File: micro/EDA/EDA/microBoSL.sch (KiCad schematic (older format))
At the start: 51 parts, among them J1 Conn_01x04, J10 MOTOR_OUT, J2 Conn_01x03, J3 Conn_01x04, J4 BATTERY CONN, J5 Conn_02x03_Odd_Even, J6 Conn_01x04, J7 MOTOR_OUT, J8 USB_B_Micro, J9 MOTOR_OUT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

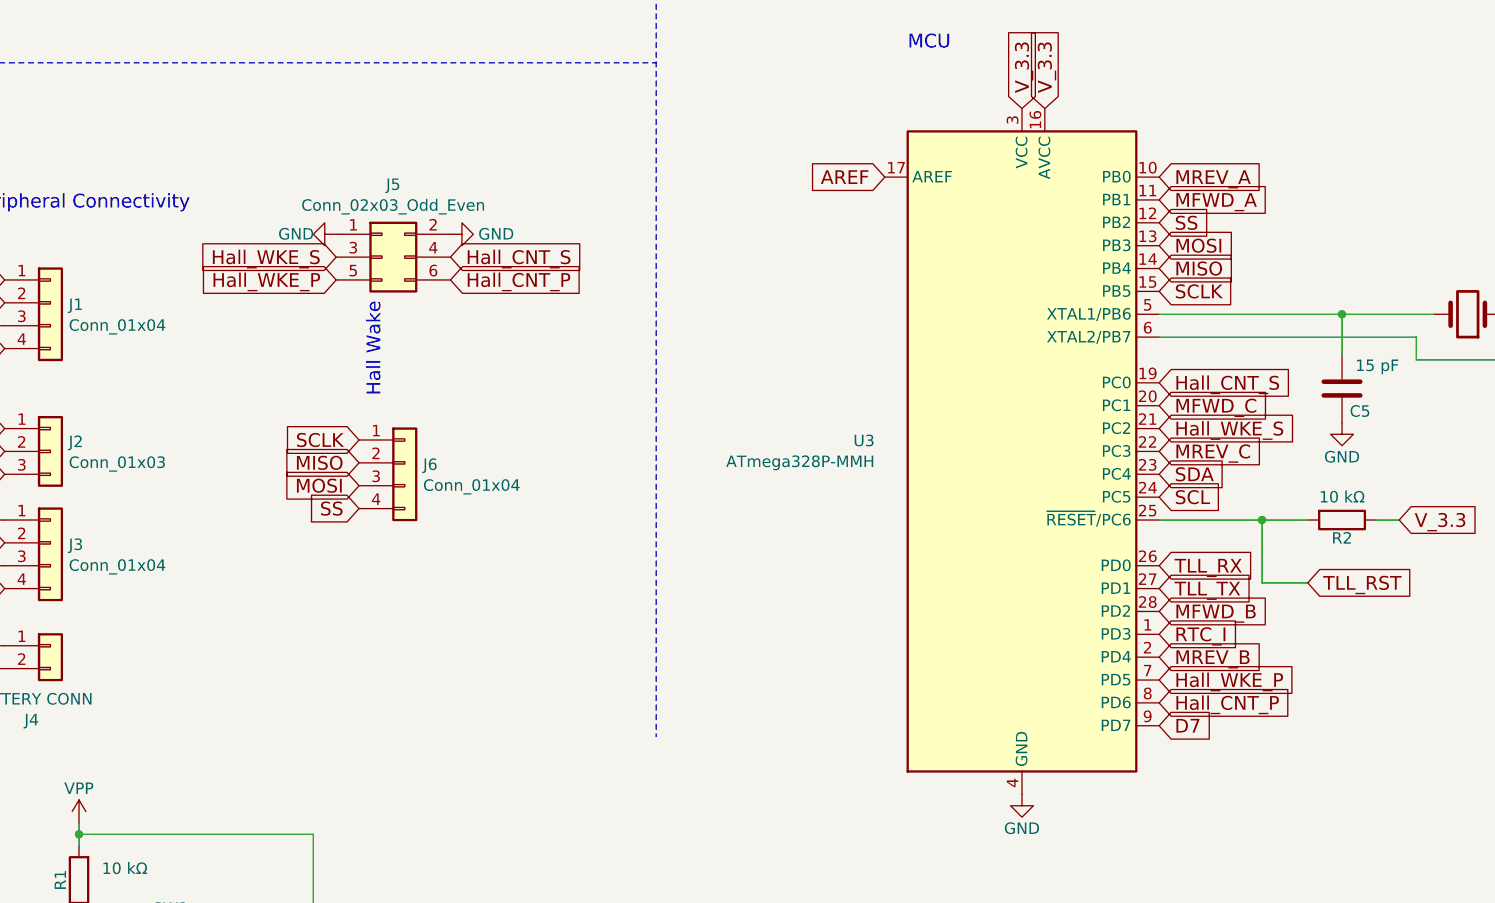
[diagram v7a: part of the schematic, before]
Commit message: routed pcb with 4 hall effect sensors, TODO silkscreen
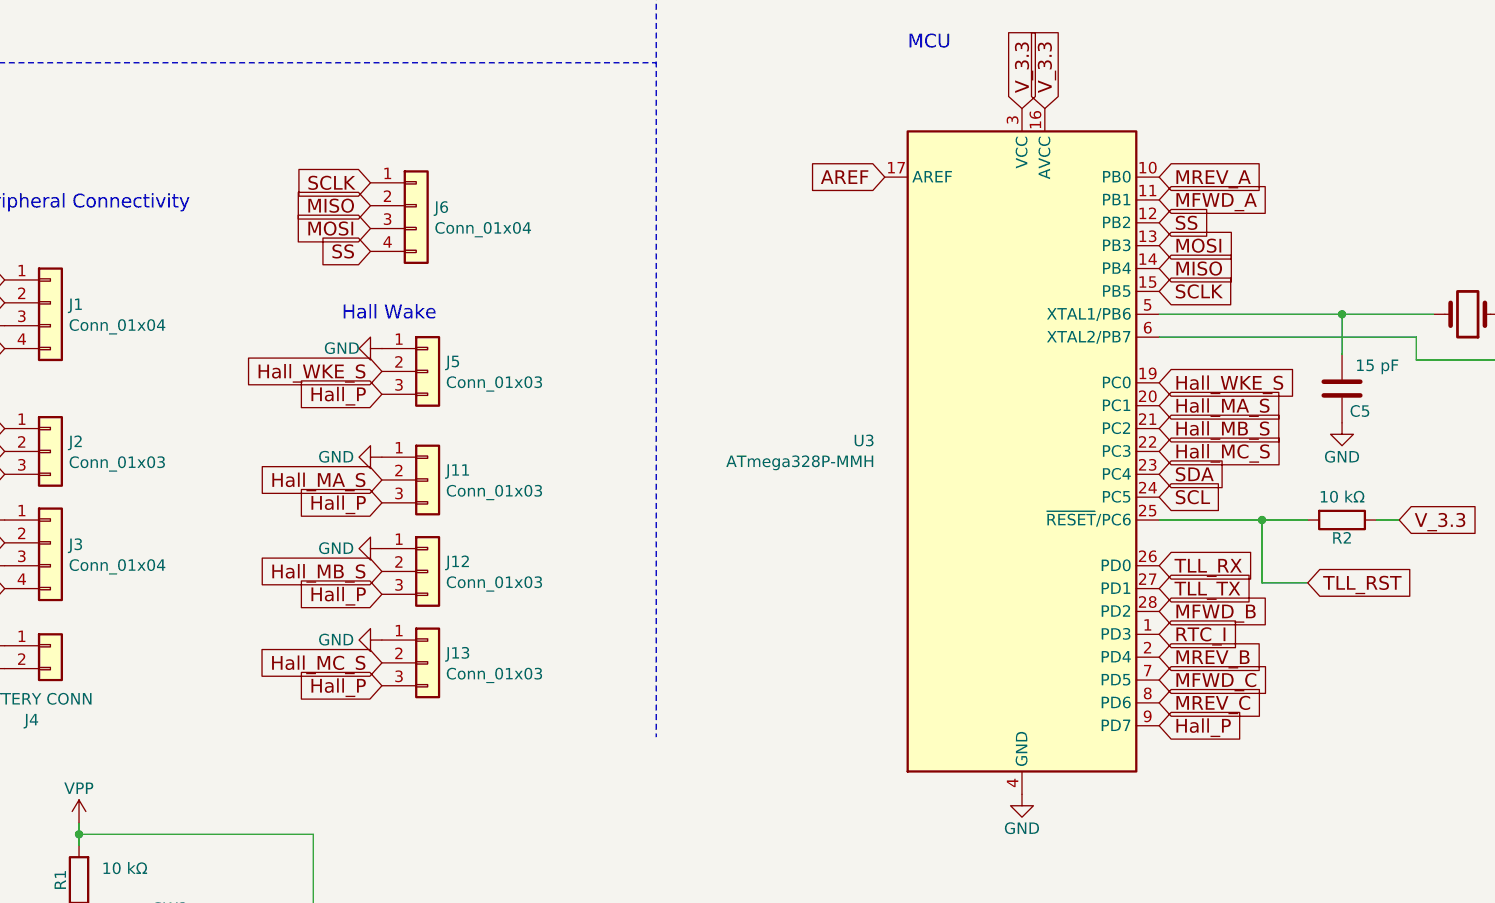
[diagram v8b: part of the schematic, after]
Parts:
- removed J5: Conn_02x03_Odd_Even, Connector_PinHeader_2.54mm:PinHeader_2x03_P2.54mm_Vertical, symbol Connector_Generic:Conn_02x03_Odd_Even
- added J11, J12, J13, J5: Conn_01x03, Connector_PinHeader_2.00mm:PinHeader_1x03_P2.00mm_Vertical, symbol Connector_Generic:Conn_01x03
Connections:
- net Hall_CNT_P is gone; now on net MREV_C: U3.8 (PD6)
- net Hall_CNT_S is gone; now on net Hall_WKE_S: U3.19 (PC0)
- net Hall_WKE_P is gone; now on net MFWD_C: U3.7 (PD5)
- net GND: now also J11.1 (Pin_1), J12.1 (Pin_1), J13.1 (Pin_1), J5.1 (Pin_1)
- net Hall_WKE_S: now also J5.2 (Pin_2); no longer U3.21 (PC2)
- net MFWD_C: no longer U3.20 (PC1)
- net MREV_C: no longer U3.22 (PC3)
- net D7 renamed Hall_P
- net Hall_P: now also J11.3 (Pin_3), J12.3 (Pin_3), J13.3 (Pin_3), J5.3 (Pin_3)
- new net Hall_MA_S: J11.2 (Pin_2), U3.20 (PC1)
- new net Hall_MB_S: J12.2 (Pin_2), U3.21 (PC2)
- new net Hall_MC_S: J13.2 (Pin_2), U3.22 (PC3)
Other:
- moved on the sheet: J6
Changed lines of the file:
@@
 	0    -1   -1   0
 $EndComp
-Text GLabel 6800 5800 2    60   Input ~ 0
-D7
 Text GLabel 5600 3400 0    60   Input ~ 0
 AREF
@@
 Text GLabel 6200 3100 1    60   Input ~ 0
 V_3.3
-Text GLabel 6800 5700 2    60   Input ~ 0
-Hall_CNT_P
+Text GLabel 6800 4600 2    60   Input ~ 0
+Hall_MC_S
 Text GLabel 14925 1475 2    60   Input ~ 0
 AND_TX
@@
 L power:GND #PWR015
 U 1 1 5FD06040
-P 3200 3650
-F 0 "#PWR015" H 3200 3400 50  0001 C CNN
-F 1 "GND" V 3200 3475 50  0000 C CNN
-F 2 "" H 3200 3650 50  0000 C CNN
-F 3 "" H 3200 3650 50  0000 C CNN
-	1    3200 3650
+P 3400 4150
+F 0 "#PWR015" H 3400 3900 50  0001 C CNN
+F 1 "GND" V 3400 3975 50  0000 C CNN
+F 2 "" H 3400 4150 50  0000 C CNN
+F 3 "" H 3400 4150 50  0000 C CNN
+	1    3400 4150
 	0    1    1    0
 $EndComp
@@
 L power:GND #PWR016
 U 1 1 5FD062CD
-P 3700 3650
-F 0 "#PWR016" H 3700 3400 50  0001 C CNN
-F 1 "GND" V 3700 3450 50  0000 C CNN
-F 2 "" H 3700 3650 50  0000 C CNN
-F 3 "" H 3700 3650 50  0000 C CNN
-	1    3700 3650
-	0    -1   -1   0
-$EndComp
-Text Notes 3400 3950 3    60   ~ 0
+P 3400 4625
+F 0 "#PWR016" H 3400 4375 50  0001 C CNN
+F 1 "GND" V 3400 4425 50  0000 C CNN
+F 2 "" H 3400 4625 50  0000 C CNN
+F 3 "" H 3400 4625 50  0000 C CNN
+	1    3400 4625
+	0    1    -1   0
+$EndComp
+Text Notes 3225 4035 0    60   ~ 0
 Hall Wake
-Text GLabel 6800 5600 2    60   Input ~ 0
-Hall_WKE_P
-Text GLabel 3200 3850 0    60   Input ~ 0
-Hall_WKE_P
-Text GLabel 3700 3850 2    60   Input ~ 0
-Hall_CNT_P
+Text GLabel 6800 4400 2    60   Input ~ 0
+Hall_MA_S
+Text GLabel 3400 4350 0    60   Input ~ 0
+Hall_P
 $Comp
 L Device:R R2
@@
 $EndComp
 Text GLabel 6800 4500 2    60   Input ~ 0
+Hall_MB_S
+Text GLabel 6800 4300 2    60   Input ~ 0
 Hall_WKE_S
-Text GLabel 6800 4300 2    60   Input ~ 0
-Hall_CNT_S
-Text GLabel 3700 3750 2    60   Input ~ 0
-Hall_CNT_S
-Text GLabel 3200 3750 0    60   Input ~ 0
+Text GLabel 3400 4725 0    60   Input ~ 0
+Hall_MA_S
+Text GLabel 3400 4250 0    60   Input ~ 0
 Hall_WKE_S
 $Comp
@@
 F 3 "~" H 1950 5000 50  0001 C CNN
 	1    1950 5000
-	1    0    0    -1
-$EndComp
-$Comp
-L Connector_Generic:Conn_02x03_Odd_Even J5
-U 1 1 5FD501D9
-P 3400 3750
-F 0 "J5" H 3450 4067 50  0000 C CNN
-F 1 "Conn_02x03_Odd_Even" H 3450 3976 50  0000 C CNN
-F 2 "Connector_PinHeader_2.54mm:PinHeader_2x03_P2.54mm_Vertical" H 3400 3750 50  0001 C CNN
-F 3 "~" H 3400 3750 50  0001 C CNN
-	1    3400 3750
 	1    0    0    -1
 $EndComp
@@
 L Connector_Generic:Conn_01x04 J6
 U 1 1 609936C2
-P 3500 4650
-F 0 "J6" H 3580 4642 50  0000 L CNN
-F 1 "Conn_01x04" H 3580 4551 50  0000 L CNN
-F 2 "Connector_PinHeader_1.27mm:PinHeader_1x04_P1.27mm_Vertical" H 3500 4650 50  0001 C CNN
-F 3 "~" H 3500 4650 50  0001 C CNN
-	1    3500 4650
-	1    0    0    -1
-$EndComp
-Text GLabel 3300 4850 0    60   Input ~ 0
+P 3550 3525
+F 0 "J6" H 3630 3517 50  0000 L CNN
+F 1 "Conn_01x04" H 3630 3426 50  0000 L CNN
+F 2 "Connector_PinHeader_1.27mm:PinHeader_1x04_P1.27mm_Vertical" H 3550 3525 50  0001 C CNN
+F 3 "~" H 3550 3525 50  0001 C CNN
+	1    3550 3525
+	1    0    0    -1
+$EndComp
+Text GLabel 3350 3725 0    60   Input ~ 0
 SS
-Text GLabel 3300 4750 0    60   Input ~ 0
+Text GLabel 3350 3625 0    60   Input ~ 0
 MOSI
-Text GLabel 3300 4650 0    60   Input ~ 0
+Text GLabel 3350 3525 0    60   Input ~ 0
 MISO
-Text GLabel 3300 4550 0    60   Input ~ 0
+Text GLabel 3350 3425 0    60   Input ~ 0
 SCLK
 $Comp
@@
 Text GLabel 6800 5500 2    60   Input ~ 0
 MREV_B
-Text GLabel 6800 4400 2    60   Input ~ 0
+Text GLabel 6800 5600 2    60   Input ~ 0
 MFWD_C
-Text GLabel 6800 4600 2    60   Input ~ 0
+Text GLabel 6800 5700 2    60   Input ~ 0
 MREV_C
+$Comp
+L Connector_Generic:Conn_01x03 J5
+U 1 1 60A95929
+P 3600 4250
+F 0 "J5" H 3680 4292 50  0000 L CNN
+F 1 "Conn_01x03" H 3680 4201 50  0000 L CNN
+F 2 "Connector_PinHeader_2.00mm:PinHeader_1x03_P2.00mm_Vertical" H 3600 4250 50  0001 C CNN
+F 3 "~" H 3600 4250 50  0001 C CNN
+	1    3600 4250
+	1    0    0    -1
+$EndComp
+$Comp
+L Connector_Generic:Conn_01x03 J11
+U 1 1 60AA85BE
+P 3600 4725
+F 0 "J11" H 3680 4767 50  0000 L CNN
+F 1 "Conn_01x03" H 3680 4676 50  0000 L CNN
+F 2 "Connector_PinHeader_2.00mm:PinHeader_1x03_P2.00mm_Vertical" H 3600 4725 50  0001 C CNN
+F 3 "~" H 3600 4725 50  0001 C CNN
+	1    3600 4725
+	1    0    0    -1
+$EndComp
+Text GLabel 3400 4825 0    60   Input ~ 0
+Hall_P
+$Comp
+L power:GND #PWR0101
+U 1 1 60AA9E45
+P 3400 5025
+F 0 "#PWR0101" H 3400 4775 50  0001 C CNN
+F 1 "GND" V 3400 4825 50  0000 C CNN
+F 2 "" H 3400 5025 50  0000 C CNN
+F 3 "" H 3400 5025 50  0000 C CNN
+	1    3400 5025
+	0    1    -1   0
+$EndComp
+Text GLabel 3400 5125 0    60   Input ~ 0
+Hall_MB_S
+$Comp
+L Connector_Generic:Conn_01x03 J12
+U 1 1 60AAA552
+P 3600 5125
+F 0 "J12" H 3680 5167 50  0000 L CNN
+F 1 "Conn_01x03" H 3680 5076 50  0000 L CNN
+F 2 "Connector_PinHeader_2.00mm:PinHeader_1x03_P2.00mm_Vertical" H 3600 5125 50  0001 C CNN
+F 3 "~" H 3600 5125 50  0001 C CNN
+	1    3600 5125
+	1    0    0    -1
+$EndComp
+Text GLabel 3400 5225 0    60   Input ~ 0
+Hall_P
+$Comp
+L power:GND #PWR0102
+U 1 1 60AAEE77
+P 3400 5425
+F 0 "#PWR0102" H 3400 5175 50  0001 C CNN
+F 1 "GND" V 3400 5225 50  0000 C CNN
+F 2 "" H 3400 5425 50  0000 C CNN
+F 3 "" H 3400 5425 50  0000 C CNN
+	1    3400 5425
+	0    1    -1   0
+$EndComp
+Text GLabel 3400 5525 0    60   Input ~ 0
+Hall_MC_S
+$Comp
+L Connector_Generic:Conn_01x03 J13
+U 1 1 60AAF5A8
+P 3600 5525
+F 0 "J13" H 3680 5567 50  0000 L CNN
+F 1 "Conn_01x03" H 3680 5476 50  0000 L CNN
+F 2 "Connector_PinHeader_2.00mm:PinHeader_1x03_P2.00mm_Vertical" H 3600 5525 50  0001 C CNN
+F 3 "~" H 3600 5525 50  0001 C CNN
+	1    3600 5525
+	1    0    0    -1
+$EndComp
+Text GLabel 3400 5625 0    60   Input ~ 0
+Hall_P
+Text GLabel 6800 5800 2    60   Input ~ 0
+Hall_P
 $EndSCHEMATC
